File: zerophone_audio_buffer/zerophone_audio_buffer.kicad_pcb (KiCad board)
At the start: 2 copper layers, 13.2 x 10.7 mm, 7 parts, among them P1 CONN_01X03, P2 CONN_01X04, U1 LM1117-2.5, U2 NC7WZ16

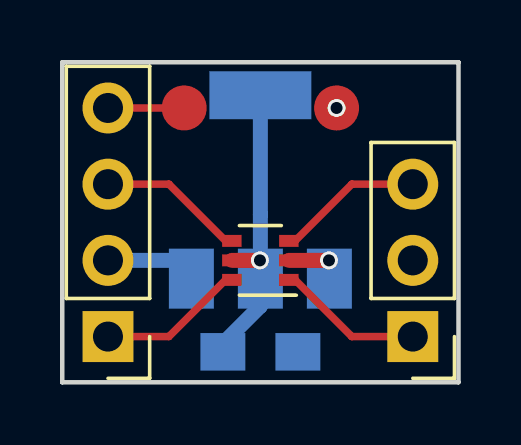
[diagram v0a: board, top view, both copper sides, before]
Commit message: Corrected buffer pinout; changed power symbols
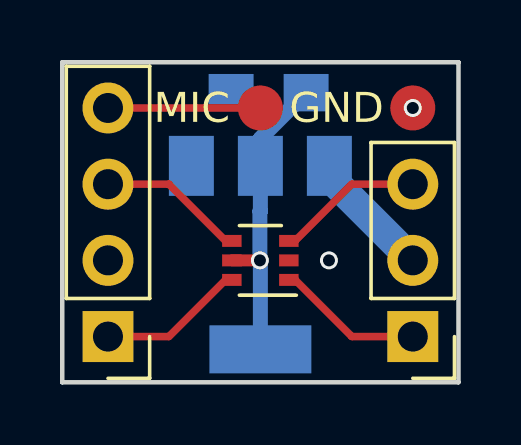
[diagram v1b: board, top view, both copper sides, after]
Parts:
- P1: value CONN_01X03 -> INPUT_CONN
- P2: value CONN_01X04 -> OUTPUT_CONN
- moved C1 8.64 mm to (132.4, 93.5), turned to 180 degrees
- moved W1 2.54 mm to (132.1, 94.0)
- moved U1 2.54 mm to (132.1, 99.1), turned to 270 degrees
- moved W2 2.54 mm to (137.2, 94.0)
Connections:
- net VDD renamed +2V5
- P1 pad 2: GND -> +3V3
- P2 pad 2: VCC -> GND
- U1 pad 3: VCC -> +3V3
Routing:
- net +3V3: track 0.00 -> 4.30 mm
- net VCC: track 3.03 -> 0.00 mm
- net Net-(P2-Pad4): track 2.54 -> 5.33 mm
- net GND: track 1.34 -> 0.00 mm, vias 2 -> 1
- net (no net): vias 0 -> 1
